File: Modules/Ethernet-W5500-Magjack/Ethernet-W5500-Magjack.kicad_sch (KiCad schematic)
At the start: 37 parts, among them J2 ARJM11C7-114-BA-EW2, U3 W5500, Y1 25.000MHz CL=12pF

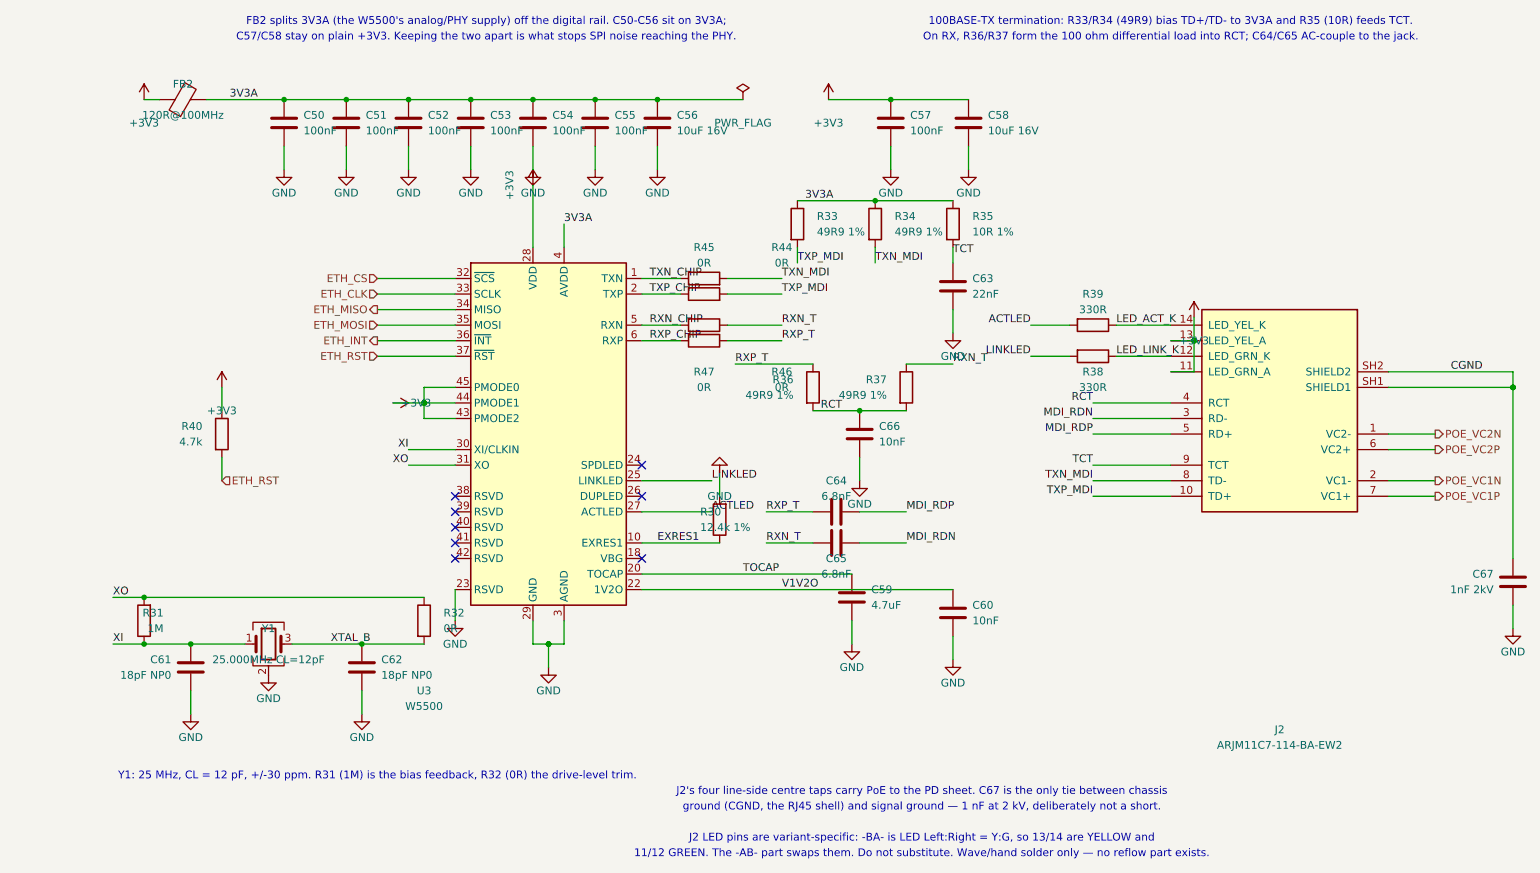
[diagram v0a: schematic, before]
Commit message: Prepare eight module boards and import their footprints
Set up the eight remaining layout blocks to the pattern of the PoE block.
Every board now holds its footprints, net classes and design rules. No
placement or routing yet.

Module projects
- Seven new projects under Modules/, from the Ethernet stub
- Each .kicad_pro binds its nets to classes. RF adds RF_50 (0.17 mm) on
  /ANT_433. USB boards add a USB pair class
- Each .kicad_dru carries the shared PCBWay rules. RF and PowerMux add a
  fanout rule. RF adds a J3 edge rule
- Update PCB from Schematic ran on all eight. check_import.py passes on
  each: same references, every class bound, the DRC canary fires

Schematic changes, each checked by a netlist membership diff
- Interface local labels are now hierarchical labels: V5_SYS, LED_*,
  USB_DP, USB_DM
- PowerMux R70 118k to 169k. PR1 reference is 1.06 V (SLVSEA3F), so the
  handover moves from 3.51 V to 4.57 V, as the note states
- Buck C100 10 uF 0805 to 22 uF 1206. The note names the TPS563208
- RF C22, C23, C29 value labels match their part numbers. U4 uses the
  stock footprint with no vias. Layout adds the 5 tented vias
- Title blocks name each block

Library policy: global rows only
- Remove the vendored PoEEthModule.pretty and every project library row.
  PoE DRC holds at 36 warnings and 0 library issues

Tooling
- check_courtyards.py and check_plan.py work on any board. 16 tests
- check_import.py, the acceptance test for GUI batch 1
- docs/Layout-Batch-Runbook.md
- A draft Layout-Spec.md for each new module

Co-Authored-By: Claude Opus 5.5 (1M context) <noreply@anthropic.com>
Claude-Session: https://claude.ai/code/session_01ErAAfkmF4h3T5yfrw21utF
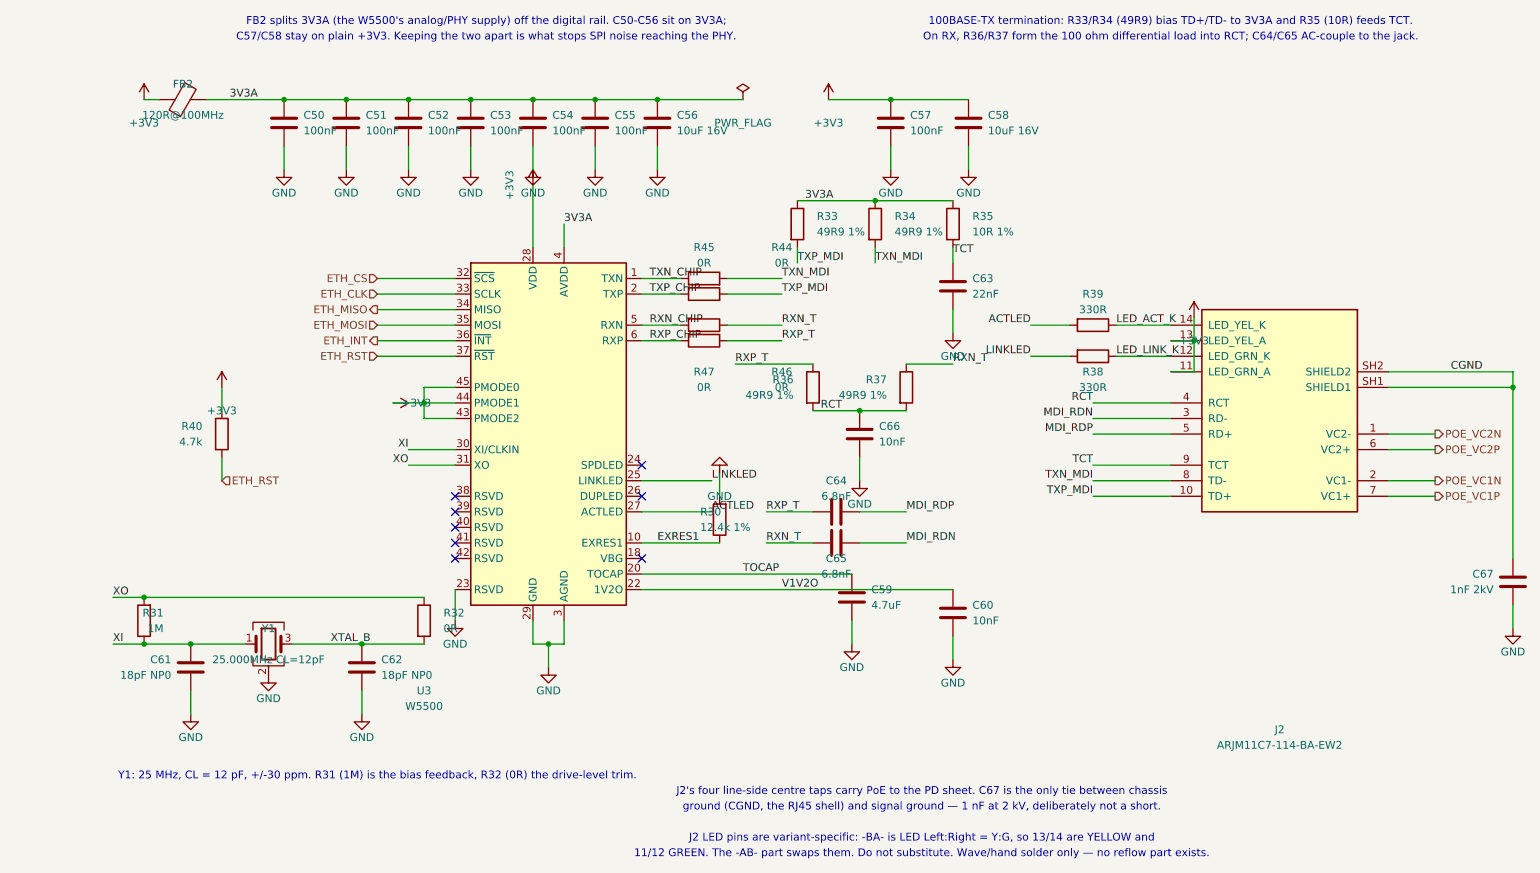
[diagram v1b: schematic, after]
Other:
- title: Plum RF Bridge -> Ethernet-W5500-Magjack
